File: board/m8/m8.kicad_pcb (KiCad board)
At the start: 2 copper layers, 50 x 25 mm, 11 parts, among them J1 program, SW1 B3F-4000, U1 CH32V003f4p6

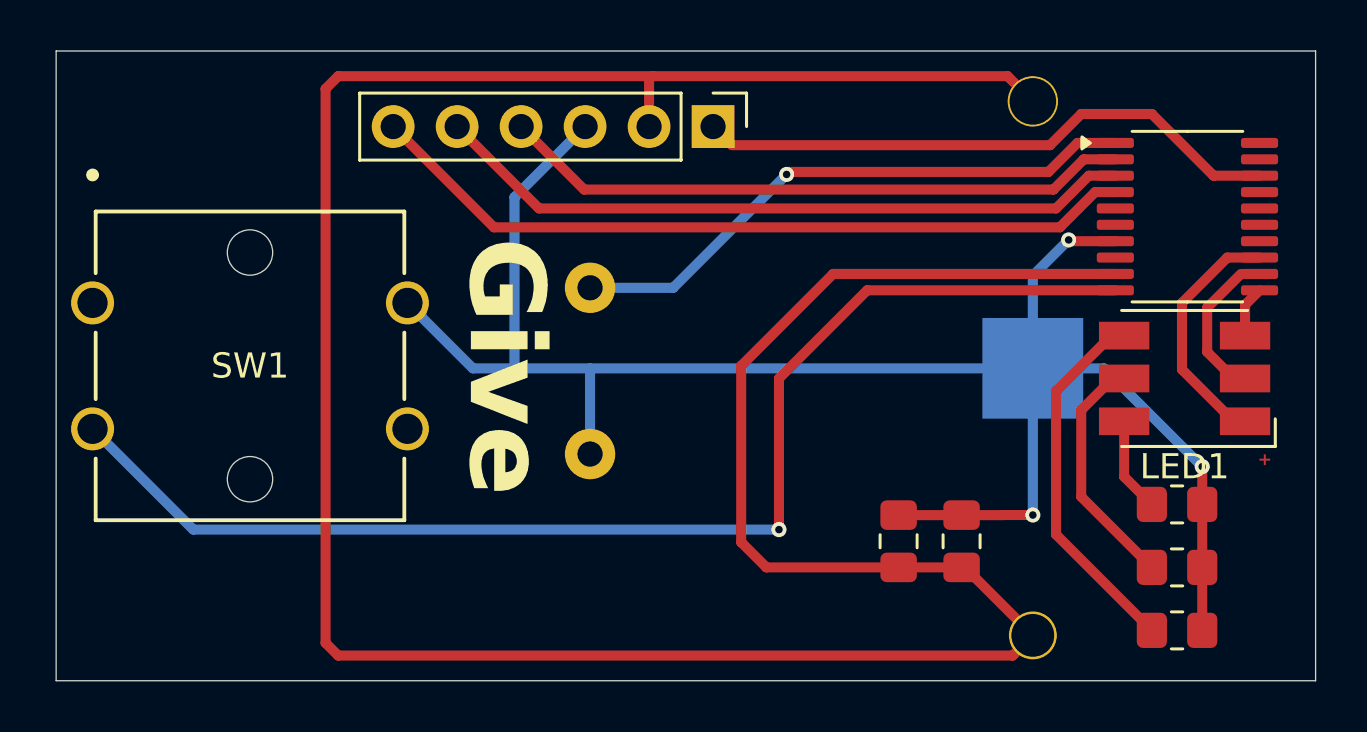
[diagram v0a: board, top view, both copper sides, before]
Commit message: increase clearances
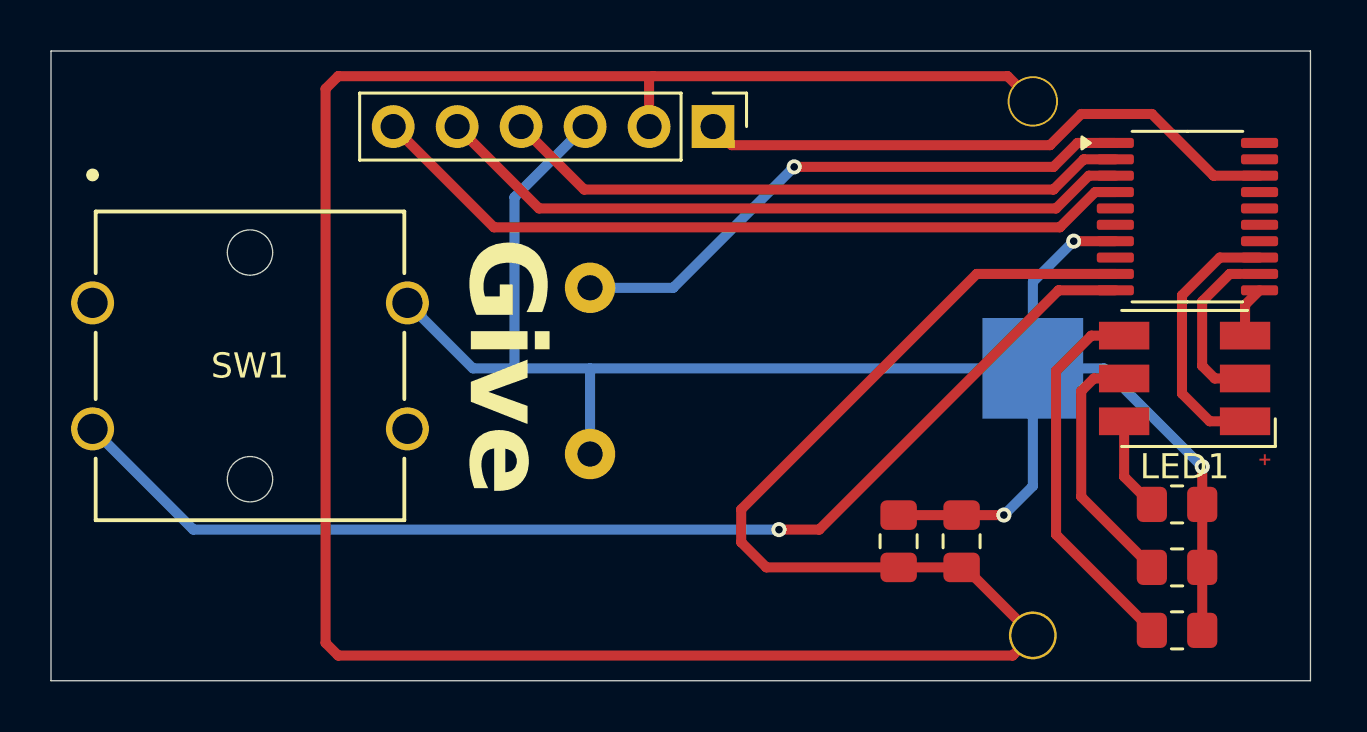
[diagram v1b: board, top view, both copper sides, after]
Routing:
- net Net-(U1-PC0_T2CH3): track 50.3 -> 46.7 mm
- net VCC: track 117.9 -> 114.5 mm
- net Net-(LED1-RA): track 8.00 -> 8.87 mm
- net GND: track 73.4 -> 72.6 mm
- net Net-(LED1-BA): track 10.3 -> 11.0 mm

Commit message: move LED down
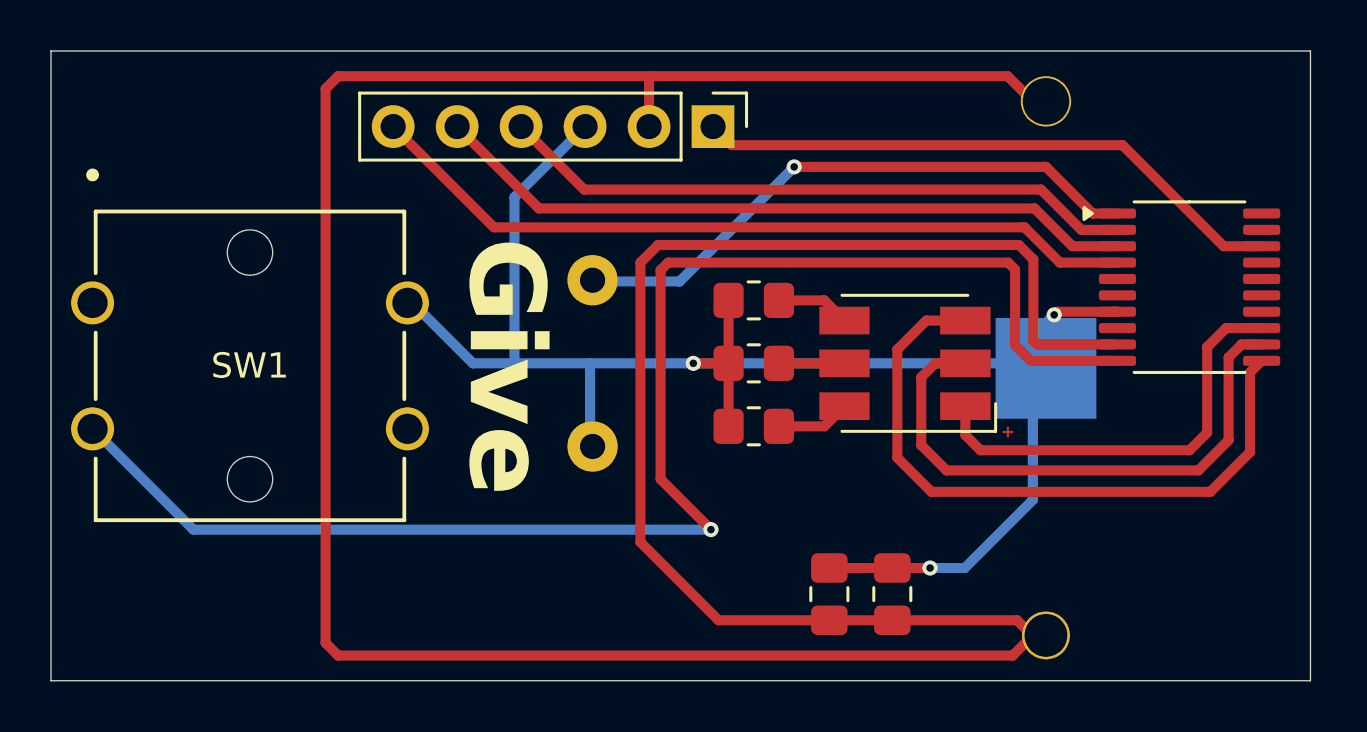
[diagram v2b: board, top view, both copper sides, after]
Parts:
- moved R1 21.3 mm to (147.5, 109.9), turned to 0 degrees
- moved R2 18.7 mm to (147.5, 112.4), turned to 0 degrees
- moved R3 17.1 mm to (147.5, 114.9), turned to 0 degrees
- moved LED1 11.1 mm to (153.5, 112.4)
- moved C1 3.46 mm to (153.0, 121.6)
- moved C2 3.46 mm to (150.5, 121.6)
- moved U1 2.80 mm to (164.8, 109.4)
- moved BT1 0.52 mm to (159.1, 112.6)
- moved LS1 0.32 mm to (141.1, 109.1)
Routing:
- net Net-(LED1-GA): track 2.04 -> 26.5 mm
- net VCC: track 114.5 -> 132.2 mm
- net Net-(LED1-RA): track 8.87 -> 23.0 mm
- net Net-(U1-PC0_T2CH3): track 46.7 -> 59.4 mm
- net Net-(LED1-GK): track 15.2 -> 2.93 mm
- net Net-(LED1-RK): track 11.2 -> 2.60 mm
- net GND: track 72.6 -> 65.9 mm
- net Net-(LED1-BA): track 11.0 -> 17.2 mm
- net Net-(LED1-BK): track 3.76 -> 2.93 mm
